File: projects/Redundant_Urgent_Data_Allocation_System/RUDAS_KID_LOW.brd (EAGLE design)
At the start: 99 x 49.2 mm, 30 parts, among them IC2 STM32F103VGT6, IC3 5M240ZT100

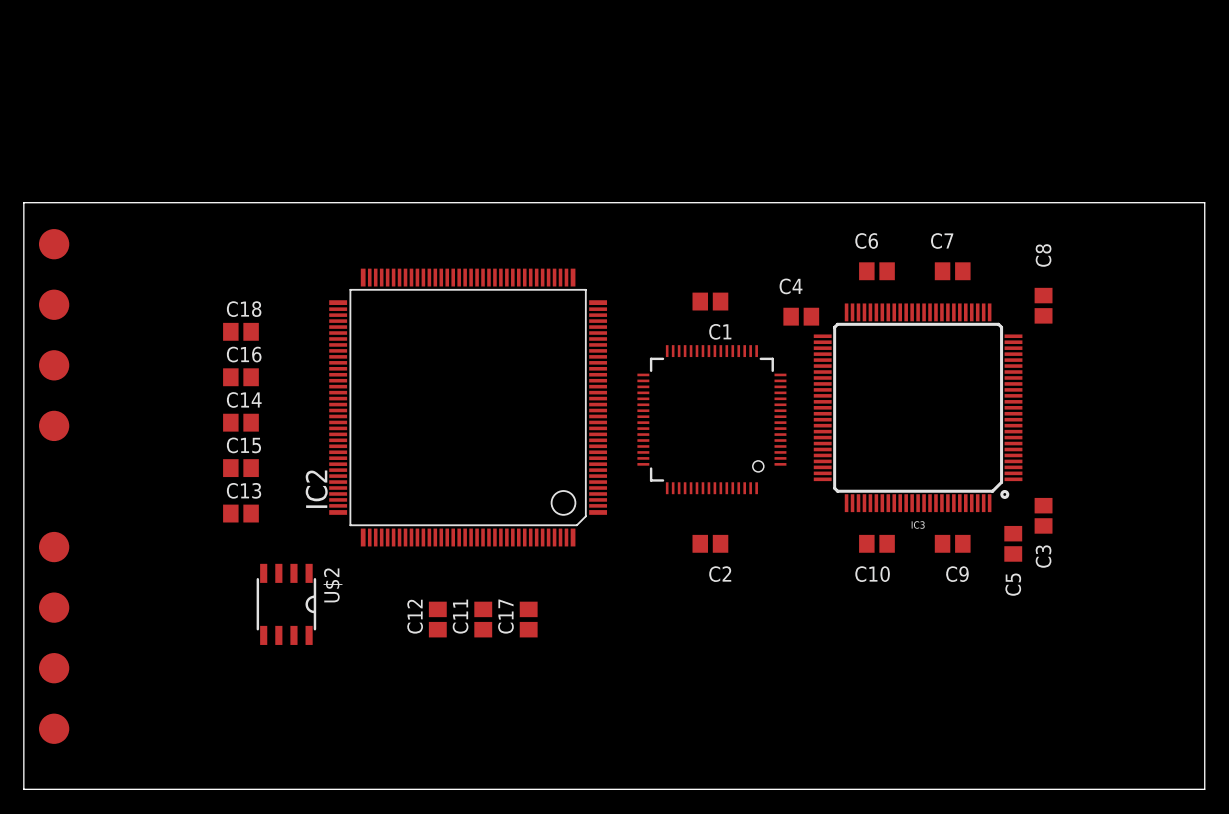
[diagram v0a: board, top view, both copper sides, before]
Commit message: add new part list
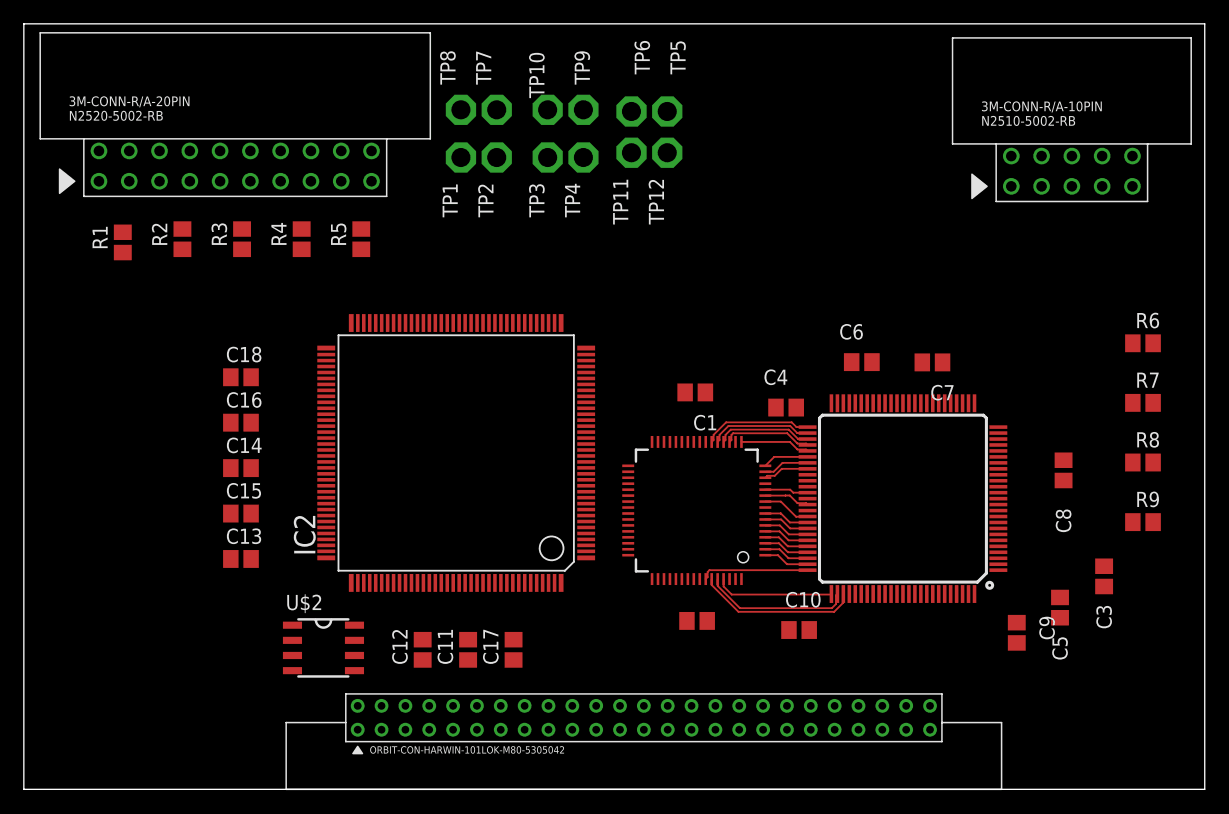
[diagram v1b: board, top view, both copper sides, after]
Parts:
- removed CAN_GND, CAN_H, CAN_L, CAN_VCC, UART_GND, UART_RX, UART_TX, UART_VCC: TP, ORBiT-special:TP_SMD
- added R1, R2, R3, R4, R5, R6, R7, R8, R9: (no value), rcl:R2012
- added TP1, TP10, TP11, TP12, TP2, TP3, TP4, TP5, TP6, TP7, TP8, TP9: TP063, ORBiT-special:TP_063
- added U$3: CONN-10PINR/A-10PIN, ORBIT-CONN HEADER-3M-2500 Series:R/A-10PIN
- added U$4: CONN-20PINR/A-20PIN, ORBIT-CONN HEADER-3M-2500 Series:R/A-20PIN
- added U$5: CARD_EDGE_50PINM80-5305042, ORBIT-CON-HARWIN-101LOK:M80-5305042
- moved C8 13.9 mm to (87.2, 26.8), turned to 270 degrees
- moved C10 9.74 mm to (65.0, 13.4), turned to 180 degrees
- moved C9 9.20 mm to (83.3, 13.1), turned to 90 degrees
- moved C7 7.83 mm to (76.2, 35.8), turned to 180 degrees
- moved C6 7.73 mm to (70.3, 35.8)
- moved U$1 7.73 mm to (56.4, 23.4)
- moved IC3 7.73 mm to (73.7, 24.4)
- moved C4 7.73 mm to (63.9, 32.0)
- moved C1 7.73 mm to (56.3, 33.3)
- moved C3 7.18 mm to (90.6, 17.9)
- moved C5 6.63 mm to (86.9, 15.2)
- moved C2 6.56 mm to (56.5, 14.1)
- moved U$2 4.80 mm to (25.1, 11.9), turned to 270 degrees
- moved IC2 3.94 mm to (36.3, 28.2)
- moved C15 3.81 mm to (18.2, 23.1)
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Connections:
- net VCC2 renamed SIGNAL_VCC
- removed net CAN_H: U$2.7
- removed net CAN_L: U$2.6
- removed net GND1: U$2.4
- removed net GND2: U$2.5
- removed net VCC1: U$2.1
- new net +12V: U$5.PIN1
- new net +3V: U$5.PIN3
- new net +5V: U$5.PIN27
- new net 12V_GND: U$5.PIN26
- new net 3V_GND: U$5.PIN28
- new net 5V_GND: U$5.PIN2
- new net CAN_H_P: U$2.7, U$5.PIN4
- new net CAN_H_S: U$5.PIN29
- new net CAN_L_P: U$2.6, U$5.PIN5
- new net CAN_L_S: U$5.PIN30
- new net CPLD_IO_VCC: R6.2, R7.2, R8.2, U$3.PIN7, U$3.PIN8
- new net CPLD_VCC_CORE: IC3.13, IC3.63
- new net CPLD_VCC_IO2: IC3.59, IC3.80, IC3.94
- new net CPL_VCC_IO1: IC3.31, IC3.45, IC3.9
- new net LAN_CLK_N0: IC3.81, U$5.PIN9
- new net LAN_CLK_N1: IC3.85, U$5.PIN15
- new net LAN_CLK_N2: IC3.96, U$5.PIN21
- new net LAN_CLK_N3: IC3.29, U$5.PIN34
- new net LAN_CLK_N4: IC3.19, U$5.PIN40
- new net LAN_CLK_N5: IC3.5, U$5.PIN46
- new net LAN_CLK_P0: IC3.82, U$5.PIN10
- new net LAN_CLK_P1: IC3.86, U$5.PIN16
- new net LAN_CLK_P2: IC3.97, U$5.PIN22
- new net LAN_CLK_P3: IC3.28, U$5.PIN35
- new net LAN_CLK_P4: IC3.18, U$5.PIN41
- new net LAN_CLK_P5: IC3.4, U$5.PIN47
- new net LAN_N0: IC3.83, U$5.PIN11
- new net LAN_N1: IC3.87, U$5.PIN17
- new net LAN_N2: IC3.98, U$5.PIN23
- new net LAN_N3: IC3.27, U$5.PIN36
- new net LAN_N4: IC3.17, U$5.PIN42
- new net LAN_N5: IC3.3, U$5.PIN48
- new net LAN_P0: IC3.84, U$5.PIN12
- new net LAN_P1: IC3.88, U$5.PIN18
- new net LAN_P2: IC3.99, U$5.PIN24
- new net LAN_P3: IC3.26, U$5.PIN37
- new net LAN_P4: IC3.16, U$5.PIN43
- new net LAN_P5: IC3.2, U$5.PIN49
- new net NOTE0: U$5.PIN13
- new net NOTE1: U$5.PIN19
- new net NOTE2: U$5.PIN25
- new net NOTE3: U$5.PIN38
- new net NOTE4: U$5.PIN44
- new net NOTE5: U$5.PIN50
- new net SIGNAL_GND: U$2.5, U$5.PIN14, U$5.PIN20, U$5.PIN33, U$5.PIN39, U$5.PIN45, U$5.PIN8
- net CPLD_GND: now also R9.1, U$3.PIN10, U$3.PIN6
- net CPLD_VCC: no longer IC3.13, IC3.31, IC3.45, IC3.59, IC3.63, IC3.80, IC3.9, IC3.94
- net C_TCK: now also R9.2, U$3.PIN1
- net C_TDI: now also R8.1, U$3.PIN5
- net C_TDO: now also R6.1, U$3.PIN2
- net C_TMS: now also R7.1, U$3.PIN3
- net STM32_CAN_RX: now also TP7.TP
- net STM32_CAN_TX: now also TP8.TP
- net STM32_I2C1_SCL: now also TP9.TP
- net STM32_I2C1_SDA: now also TP10.TP
- net STM32_SPI1_CS: now also TP1.TP
- net STM32_SPI1_MISO: now also TP3.TP
- net STM32_SPI1_MOSI: now also TP4.TP
- net STM32_SPI1_SCK: now also TP2.TP
- net STM32_UART1_RX: now also TP6.TP; no longer UART_RX.P$1
- net STM32_UART1_TX: now also TP5.TP; no longer UART_TX.P$1
- net STM32_UART2_RX: now also TP12.TP
- net STM32_UART2_TX: now also TP11.TP
- net S_GND: now also R5.1, U$2.4, U$4.PIN12, U$4.PIN13, U$4.PIN14, U$4.PIN15, U$4.PIN16, U$4.PIN17, U$4.PIN18, U$4.PIN19, U$4.PIN20
- net S_RST: now also U$4.PIN9
- net S_TCK: now also R5.2, U$4.PIN5
- net S_TDI: now also R2.1, U$4.PIN3
- net S_TDO: now also R4.1, U$4.PIN7
- net S_TMS: now also R3.1, U$4.PIN4
- net S_TRST: now also R1.1, U$4.PIN2
- net S_VCC: now also R1.2, R2.2, R3.2, R4.2, U$2.1, U$4.PIN1, U$4.PIN11
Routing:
- net R/!W!: track 0.00 -> 13.5 mm
- net !BUSY!: track 0.00 -> 12.3 mm
- net !INT!: track 0.00 -> 9.98 mm
- net D7: track 0.00 -> 9.14 mm
- net !CE!: track 0.00 -> 9.11 mm
- net D6: track 0.00 -> 8.60 mm
- net D5: track 0.00 -> 8.05 mm
- net D4: track 0.00 -> 7.51 mm
- net D3: track 0.00 -> 5.86 mm
- net A7: track 0.00 -> 4.08 mm
- net A8: track 0.00 -> 3.86 mm
- net A6: track 0.00 -> 3.86 mm
- net A5: track 0.00 -> 3.86 mm
- net A4: track 0.00 -> 3.86 mm
- net A2: track 0.00 -> 3.86 mm
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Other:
- board size 99 x 49.2 mm -> 99 x 64.2 mm

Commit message: add
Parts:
- moved TP1 10.2 mm to (46.8, 53.0)
- moved TP10 10.2 mm to (54.1, 57.0)
- moved TP12 10.2 mm to (64.1, 53.4)
- moved TP2 10.2 mm to (49.8, 53.0)
- moved TP3 10.2 mm to (54.1, 53.0)
- moved TP4 10.2 mm to (57.1, 53.0)
- moved TP5 10.2 mm to (64.1, 56.9)
- moved TP7 10.2 mm to (49.8, 57.0)
- moved TP8 10.2 mm to (46.8, 57.0)
- moved TP9 10.2 mm to (57.1, 57.0)
- moved TP11 10.2 mm to (61.1, 53.4)
- moved TP6 10.2 mm to (61.1, 56.9)

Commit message: chage
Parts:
- moved R6 6.48 mm to (95.1, 43.8)
- moved R7 6.48 mm to (95.1, 38.8)
- moved R9 6.48 mm to (95.1, 28.8)
- moved R8 6.48 mm to (95.1, 33.8)
- moved U$2 1.27 mm to (25.1, 13.1)
